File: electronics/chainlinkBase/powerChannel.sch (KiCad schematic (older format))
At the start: 15 parts, among them J201 CHANNEL, U201 INA219BxD, U202 VN7007ALH

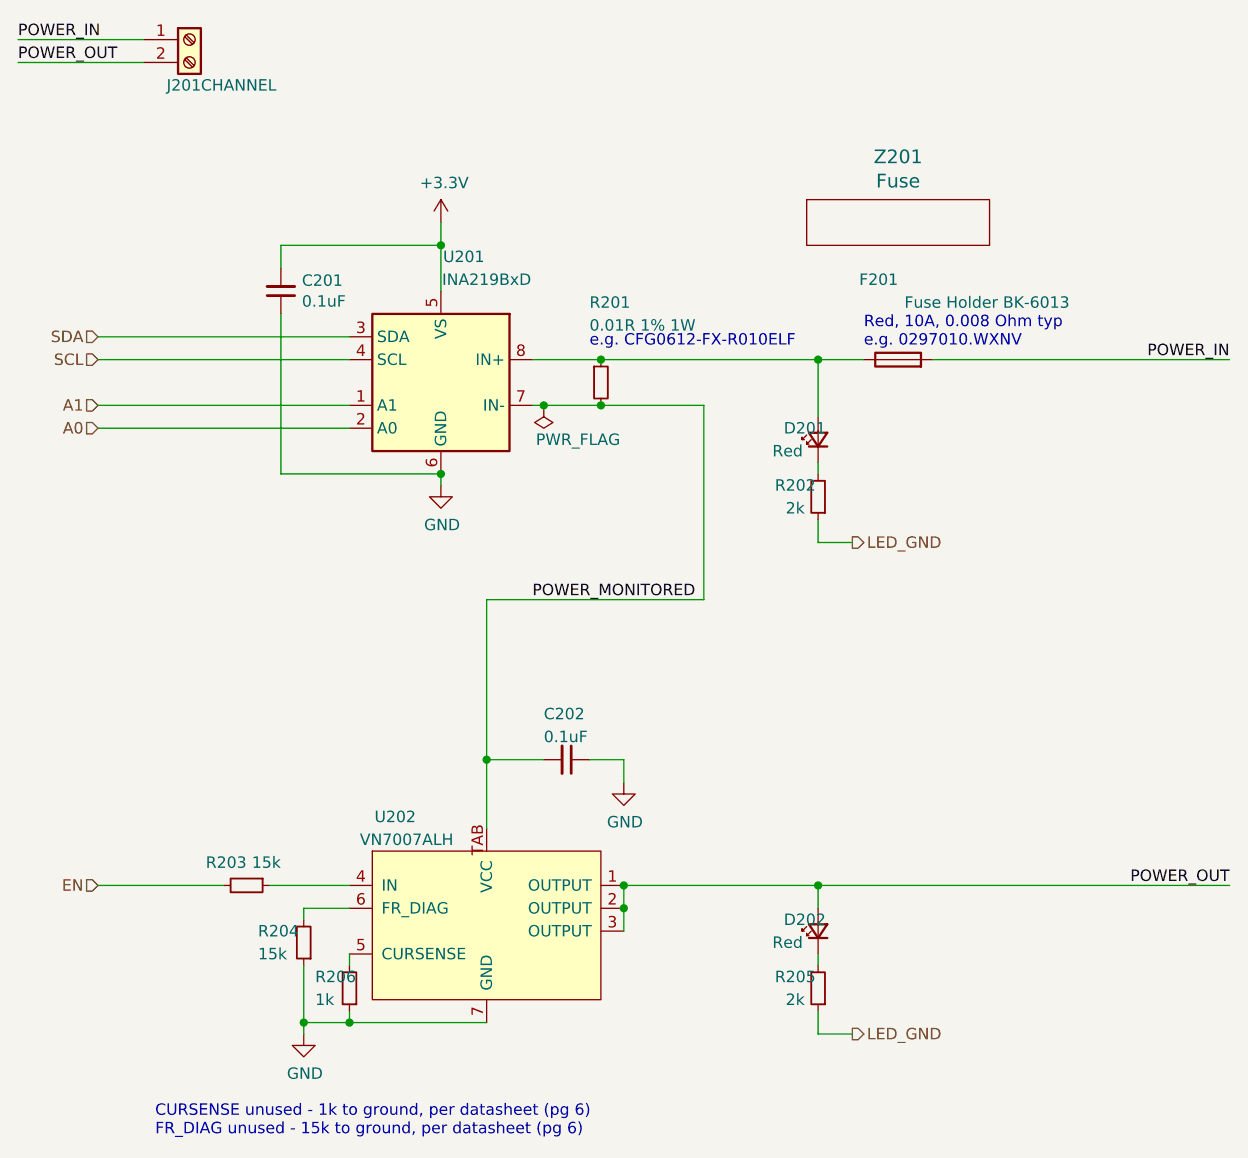
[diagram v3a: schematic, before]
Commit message: Add pull-down for load switches, move LED jumpers and make solder-bridgeable
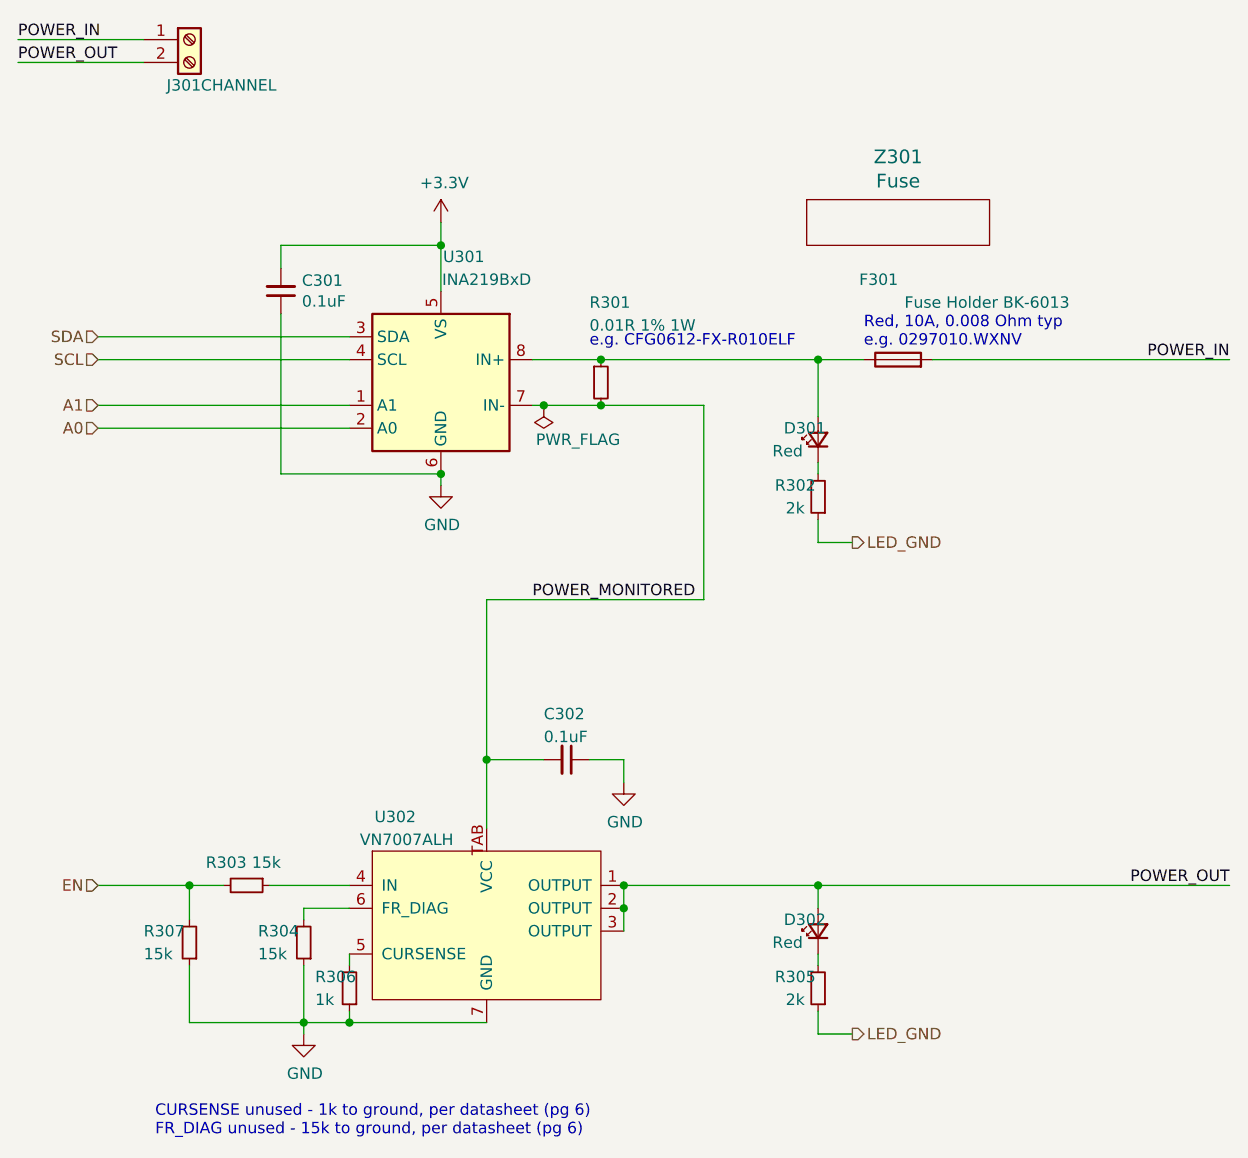
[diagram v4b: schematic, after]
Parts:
- added R207: 15k, Resistor_SMD:R_0805_2012Metric, symbol Device:R_Small
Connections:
- net EN: now also R207.2
- net GND: now also R207.1
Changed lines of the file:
@@
 $Descr A4 11693 8268
 encoding utf-8
-Sheet 2 6
+Sheet 3 6
 Title ""
 Date ""
@@
 AR Path="/60B0E338/60718742" Ref="C501"  Part="1"
 AR Path="/60B1F5E9/60718742" Ref="C601"  Part="1"
-F 0 "C201" H 2208 1804 50  0000 R CNN
+F 0 "C301" H 2208 1804 50  0000 R CNN
 F 1 "0.1uF" H 2208 1895 50  0000 R CNN
 F 2 "Capacitor_SMD:C_0805_2012Metric" H 2300 1850 50  0001 C CNN
@@
 AR Path="/60B0E338/6071874C" Ref="D502"  Part="1"
 AR Path="/60B1F5E9/6071874C" Ref="D602"  Part="1"
-F 0 "D202" V 4700 4800 50  0000 R CNN
+F 0 "D302" V 4700 4800 50  0000 R CNN
 F 1 "Red" V 4600 4850 50  0000 R CNN
 F 2 "ModifiedSymbols:LED_0805_2012Metric_Silkscreen" V 4650 4650 50  0001 C CNN
@@
 AR Path="/60B0E338/60718758" Ref="R505"  Part="1"
 AR Path="/60B1F5E9/60718758" Ref="R605"  Part="1"
-F 0 "R205" H 4750 4850 50  0000 C CNN
+F 0 "R305" H 4750 4850 50  0000 C CNN
 F 1 "2k" H 4750 4950 50  0000 C CNN
 F 2 "Resistor_SMD:R_0805_2012Metric" H 4650 4900 50  0001 C CNN
@@
 AR Path="/60B0E338/6071875F" Ref="C502"  Part="1"
 AR Path="/60B1F5E9/6071875F" Ref="C602"  Part="1"
-F 0 "C202" V 3350 3800 50  0000 L CNN
+F 0 "C302" V 3350 3800 50  0000 L CNN
 F 1 "0.1uF" V 3450 3800 50  0000 L CNN
 F 2 "Capacitor_SMD:C_0805_2012Metric" H 3550 3900 50  0001 C CNN
@@
 AR Path="/60B0E338/6071877C" Ref="R501"  Part="1"
 AR Path="/60B1F5E9/6071877C" Ref="R601"  Part="1"
-F 0 "R201" H 3650 2600 50  0000 L CNN
+F 0 "R301" H 3650 2600 50  0000 L CNN
 F 1 "0.01R 1% 1W" H 3650 2500 50  0000 L CNN
 F 2 "Resistor_SMD:R_0612_1632Metric" H 3700 2250 50  0001 C CNN
@@
 AR Path="/60B0E338/60718784" Ref="F501"  Part="1"
 AR Path="/60B1F5E9/60718784" Ref="F601"  Part="1"
-F 0 "F201" V 5350 2150 50  0000 L CNN
+F 0 "F301" V 5350 2150 50  0000 L CNN
 F 1 "Fuse Holder BK-6013" V 5250 1400 50  0000 L CNN
 F 2 "BK-6013:BK-6013" V 4930 2150 50  0001 C CNN
@@
 AR Path="/60B0E338/6071879D" Ref="R503"  Part="1"
 AR Path="/60B1F5E9/6071879D" Ref="R603"  Part="1"
-F 0 "R203" V 2050 4450 50  0000 R CNN
+F 0 "R303" V 2050 4450 50  0000 R CNN
 F 1 "15k" V 2050 4600 50  0000 R CNN
 F 2 "Resistor_SMD:R_0805_2012Metric" H 2150 4450 50  0001 C CNN
@@
 AR Path="/60B0E338/607187A4" Ref="J501"  Part="1"
 AR Path="/60B1F5E9/607187A4" Ref="J601"  Part="1"
-F 0 "J201" H 1800 550 50  0000 L CNN
+F 0 "J301" H 1800 550 50  0000 L CNN
 F 1 "CHANNEL" H 1950 550 50  0000 L CNN
 F 2 "ScrewTerminals:Generic-5.08-2P" H 1900 750 50  0001 C CNN
@@
 AR Path="/60B0E338/607187B2" Ref="U502"  Part="1"
 AR Path="/60B1F5E9/607187B2" Ref="U602"  Part="1"
-F 0 "U202" H 2800 4950 50  0000 C CNN
+F 0 "U302" H 2800 4950 50  0000 C CNN
 F 1 "VN7007ALH" H 2850 4850 50  0000 C CNN
 F 2 "VN7007ALHTR:VN7007ALHTR" H 3200 4550 50  0001 C CNN
@@
 AR Path="/60B0E338/607187BF" Ref="R506"  Part="1"
 AR Path="/60B1F5E9/607187BF" Ref="R606"  Part="1"
-F 0 "R206" H 2750 4850 50  0000 R CNN
+F 0 "R306" H 2750 4850 50  0000 R CNN
 F 1 "1k" H 2750 4950 50  0000 R CNN
 F 2 "Resistor_SMD:R_0805_2012Metric" H 2600 4900 50  0001 C CNN
@@
 AR Path="/60B0E338/607187C9" Ref="R504"  Part="1"
 AR Path="/60B1F5E9/607187C9" Ref="R604"  Part="1"
-F 0 "R204" H 2600 4650 50  0000 R CNN
+F 0 "R304" H 2600 4650 50  0000 R CNN
 F 1 "15k" H 2600 4750 50  0000 R CNN
 F 2 "Resistor_SMD:R_0805_2012Metric" H 2400 4700 50  0001 C CNN
@@
 AR Path="/60B0E338/607187E7" Ref="D501"  Part="1"
 AR Path="/60B1F5E9/607187E7" Ref="D601"  Part="1"
-F 0 "D201" V 4700 2650 50  0000 R CNN
+F 0 "D301" V 4700 2650 50  0000 R CNN
 F 1 "Red" V 4600 2700 50  0000 R CNN
 F 2 "ModifiedSymbols:LED_0805_2012Metric_Silkscreen" V 4650 2500 50  0001 C CNN
@@
 AR Path="/60B0E338/607187ED" Ref="R502"  Part="1"
 AR Path="/60B1F5E9/607187ED" Ref="R602"  Part="1"
-F 0 "R202" H 4750 2700 50  0000 C CNN
+F 0 "R302" H 4750 2700 50  0000 C CNN
 F 1 "2k" H 4750 2800 50  0000 C CNN
 F 2 "Resistor_SMD:R_0805_2012Metric" H 4650 2750 50  0001 C CNN
@@
 AR Path="/60B0E338/6071873C" Ref="U501"  Part="1"
 AR Path="/60B1F5E9/6071873C" Ref="U601"  Part="1"
-F 0 "U201" H 2900 2800 50  0000 C CNN
+F 0 "U301" H 2900 2800 50  0000 C CNN
 F 1 "INA219BxD" H 2800 2700 50  0000 C CNN
 F 2 "Package_SO:SOIC-8_3.9x4.9mm_P1.27mm" H 3800 1900 50  0001 C CNN
@@
 	3200 3200 3200 3900
 Wire Wire Line
-	1500 4450 2050 4450
+	1500 4450 1900 4450
 Wire Wire Line
 	4650 4550 4650 4450
@@
 AR Path="/60B0E338/6078F8EB" Ref="Z501"  Part="1"
 AR Path="/60B1F5E9/6078F8EB" Ref="Z601"  Part="1"
-F 0 "Z201" H 5000 1837 60  0000 C CNN
+F 0 "Z301" H 5000 1837 60  0000 C CNN
 F 1 "Fuse" H 5000 1731 60  0000 C CNN
 F 2 "Dummy:Dummy" H 5000 1550 60  0001 C CNN
@@
 	1    0    0    -1
 $EndComp
+$Comp
+L Device:R_Small R?
+U 1 1 607F8CFF
+P 1900 4700
+AR Path="/607F8CFF" Ref="R?"  Part="1"
+AR Path="/606FA86C/607F8CFF" Ref="R207"  Part="1"
+AR Path="/6077A779/607F8CFF" Ref="R?"  Part="1"
+AR Path="/60AEE6BF/607F8CFF" Ref="R307"  Part="1"
+AR Path="/60AFE278/607F8CFF" Ref="R407"  Part="1"
+AR Path="/60B0E338/607F8CFF" Ref="R507"  Part="1"
+AR Path="/60B1F5E9/607F8CFF" Ref="R607"  Part="1"
+F 0 "R307" H 2100 4650 50  0000 R CNN
+F 1 "15k" H 2100 4750 50  0000 R CNN
+F 2 "Resistor_SMD:R_0805_2012Metric" H 1900 4700 50  0001 C CNN
+F 3 "~" H 1900 4700 50  0001 C CNN
+F 4 "RMCF0805JT15K0CT-ND" H 1900 4700 50  0001 C CNN "DK#"
+	1    1900 4700
+	-1   0    0    1
+$EndComp
+Wire Wire Line
+	1900 4450 1900 4600
+Connection ~ 1900 4450
+Wire Wire Line
+	1900 4450 2050 4450
+Wire Wire Line
+	1900 4800 1900 5050
+Wire Wire Line
+	1900 5050 2400 5050
 $EndSCHEMATC

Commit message: Change Chainlink data connections from screw terminals to IDC (#189)
- Replace screw terminals with 2x4 IDC connectors (alternating ground) on Driver, Base, and Tester. Fixes #179
- Change Chainlink Driver Tester to all 1mm pogo pins
- Create new "Buddy" boards for connecting IDC/ribbon cable to T-Display or a breadboard
- Big readme cleanup and reorganization for clarity (hopefully!)
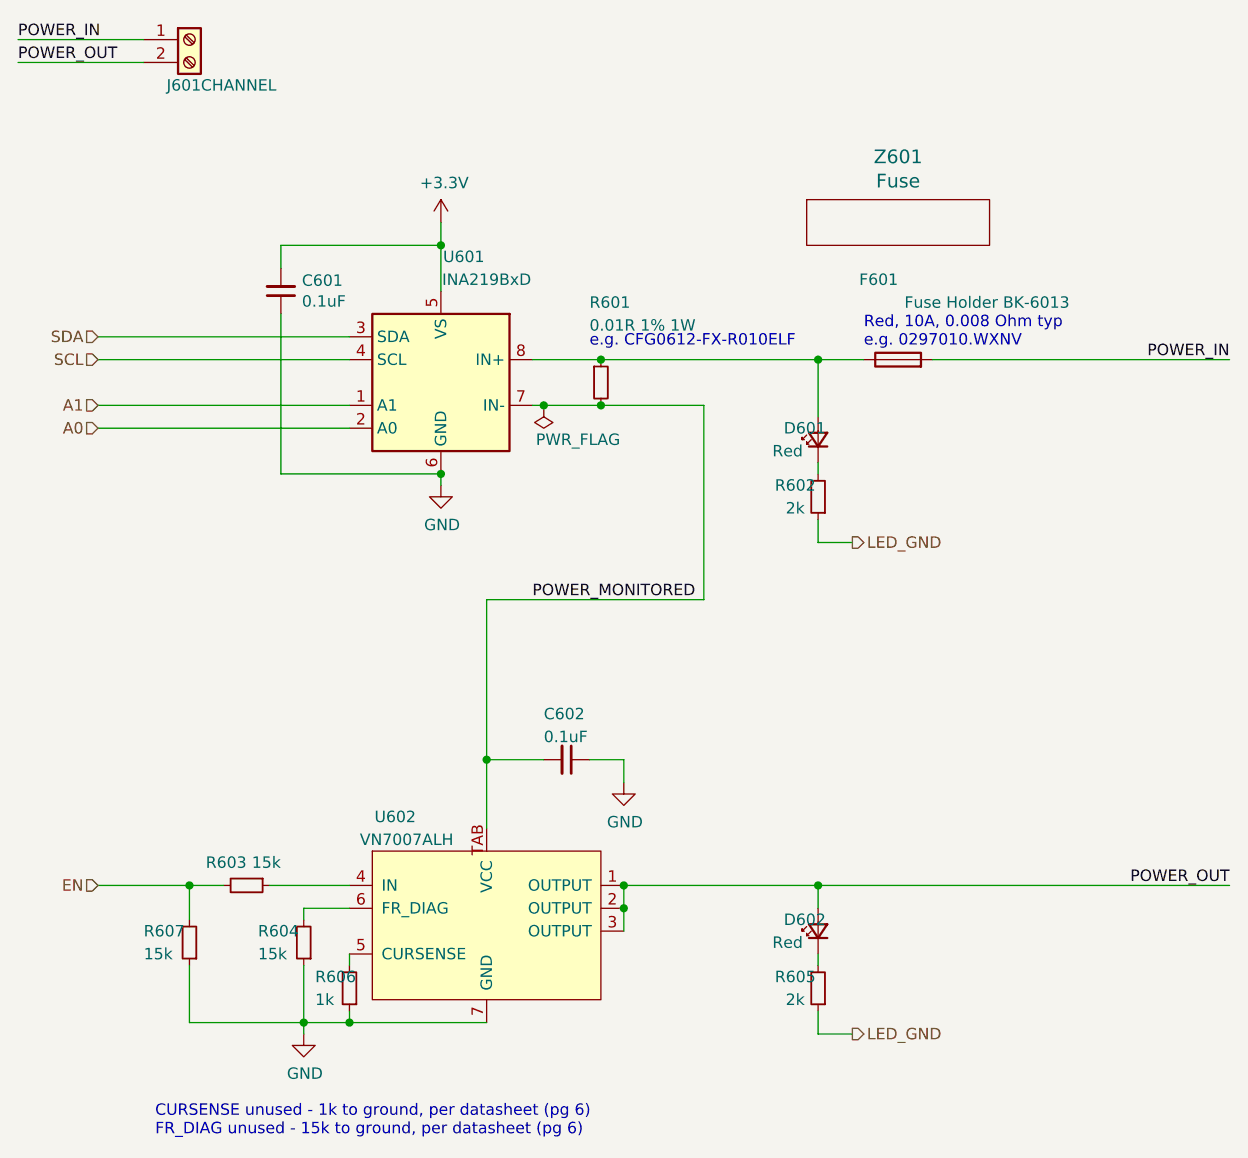
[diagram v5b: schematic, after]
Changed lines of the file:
@@
 AR Path="/60B0E338/60718742" Ref="C501"  Part="1"
 AR Path="/60B1F5E9/60718742" Ref="C601"  Part="1"
-F 0 "C301" H 2208 1804 50  0000 R CNN
+F 0 "C601" H 2208 1804 50  0000 R CNN
 F 1 "0.1uF" H 2208 1895 50  0000 R CNN
 F 2 "Capacitor_SMD:C_0805_2012Metric" H 2300 1850 50  0001 C CNN
@@
 AR Path="/60B0E338/6071874C" Ref="D502"  Part="1"
 AR Path="/60B1F5E9/6071874C" Ref="D602"  Part="1"
-F 0 "D302" V 4700 4800 50  0000 R CNN
+F 0 "D602" V 4700 4800 50  0000 R CNN
 F 1 "Red" V 4600 4850 50  0000 R CNN
 F 2 "ModifiedSymbols:LED_0805_2012Metric_Silkscreen" V 4650 4650 50  0001 C CNN
@@
 AR Path="/60B0E338/60718758" Ref="R505"  Part="1"
 AR Path="/60B1F5E9/60718758" Ref="R605"  Part="1"
-F 0 "R305" H 4750 4850 50  0000 C CNN
+F 0 "R605" H 4750 4850 50  0000 C CNN
 F 1 "2k" H 4750 4950 50  0000 C CNN
 F 2 "Resistor_SMD:R_0805_2012Metric" H 4650 4900 50  0001 C CNN
@@
 AR Path="/60B0E338/6071875F" Ref="C502"  Part="1"
 AR Path="/60B1F5E9/6071875F" Ref="C602"  Part="1"
-F 0 "C302" V 3350 3800 50  0000 L CNN
+F 0 "C602" V 3350 3800 50  0000 L CNN
 F 1 "0.1uF" V 3450 3800 50  0000 L CNN
 F 2 "Capacitor_SMD:C_0805_2012Metric" H 3550 3900 50  0001 C CNN
@@
 AR Path="/60B0E338/6071877C" Ref="R501"  Part="1"
 AR Path="/60B1F5E9/6071877C" Ref="R601"  Part="1"
-F 0 "R301" H 3650 2600 50  0000 L CNN
+F 0 "R601" H 3650 2600 50  0000 L CNN
 F 1 "0.01R 1% 1W" H 3650 2500 50  0000 L CNN
 F 2 "Resistor_SMD:R_0612_1632Metric" H 3700 2250 50  0001 C CNN
@@
 AR Path="/60B0E338/60718784" Ref="F501"  Part="1"
 AR Path="/60B1F5E9/60718784" Ref="F601"  Part="1"
-F 0 "F301" V 5350 2150 50  0000 L CNN
+F 0 "F601" V 5350 2150 50  0000 L CNN
 F 1 "Fuse Holder BK-6013" V 5250 1400 50  0000 L CNN
 F 2 "BK-6013:BK-6013" V 4930 2150 50  0001 C CNN
@@
 AR Path="/60B0E338/6071879D" Ref="R503"  Part="1"
 AR Path="/60B1F5E9/6071879D" Ref="R603"  Part="1"
-F 0 "R303" V 2050 4450 50  0000 R CNN
+F 0 "R603" V 2050 4450 50  0000 R CNN
 F 1 "15k" V 2050 4600 50  0000 R CNN
 F 2 "Resistor_SMD:R_0805_2012Metric" H 2150 4450 50  0001 C CNN
@@
 AR Path="/60B0E338/607187A4" Ref="J501"  Part="1"
 AR Path="/60B1F5E9/607187A4" Ref="J601"  Part="1"
-F 0 "J301" H 1800 550 50  0000 L CNN
+F 0 "J601" H 1800 550 50  0000 L CNN
 F 1 "CHANNEL" H 1950 550 50  0000 L CNN
 F 2 "ScrewTerminals:Generic-5.08-2P" H 1900 750 50  0001 C CNN
@@
 AR Path="/60B0E338/607187B2" Ref="U502"  Part="1"
 AR Path="/60B1F5E9/607187B2" Ref="U602"  Part="1"
-F 0 "U302" H 2800 4950 50  0000 C CNN
+F 0 "U602" H 2800 4950 50  0000 C CNN
 F 1 "VN7007ALH" H 2850 4850 50  0000 C CNN
 F 2 "VN7007ALHTR:VN7007ALHTR" H 3200 4550 50  0001 C CNN
@@
 AR Path="/60B0E338/607187BF" Ref="R506"  Part="1"
 AR Path="/60B1F5E9/607187BF" Ref="R606"  Part="1"
-F 0 "R306" H 2750 4850 50  0000 R CNN
+F 0 "R606" H 2750 4850 50  0000 R CNN
 F 1 "1k" H 2750 4950 50  0000 R CNN
 F 2 "Resistor_SMD:R_0805_2012Metric" H 2600 4900 50  0001 C CNN
@@
 AR Path="/60B0E338/607187C9" Ref="R504"  Part="1"
 AR Path="/60B1F5E9/607187C9" Ref="R604"  Part="1"
-F 0 "R304" H 2600 4650 50  0000 R CNN
+F 0 "R604" H 2600 4650 50  0000 R CNN
 F 1 "15k" H 2600 4750 50  0000 R CNN
 F 2 "Resistor_SMD:R_0805_2012Metric" H 2400 4700 50  0001 C CNN
@@
 AR Path="/60B0E338/607187E7" Ref="D501"  Part="1"
 AR Path="/60B1F5E9/607187E7" Ref="D601"  Part="1"
-F 0 "D301" V 4700 2650 50  0000 R CNN
+F 0 "D601" V 4700 2650 50  0000 R CNN
 F 1 "Red" V 4600 2700 50  0000 R CNN
 F 2 "ModifiedSymbols:LED_0805_2012Metric_Silkscreen" V 4650 2500 50  0001 C CNN
@@
 AR Path="/60B0E338/607187ED" Ref="R502"  Part="1"
 AR Path="/60B1F5E9/607187ED" Ref="R602"  Part="1"
-F 0 "R302" H 4750 2700 50  0000 C CNN
+F 0 "R602" H 4750 2700 50  0000 C CNN
 F 1 "2k" H 4750 2800 50  0000 C CNN
 F 2 "Resistor_SMD:R_0805_2012Metric" H 4650 2750 50  0001 C CNN
@@
 AR Path="/60B0E338/6071873C" Ref="U501"  Part="1"
 AR Path="/60B1F5E9/6071873C" Ref="U601"  Part="1"
-F 0 "U301" H 2900 2800 50  0000 C CNN
+F 0 "U601" H 2900 2800 50  0000 C CNN
 F 1 "INA219BxD" H 2800 2700 50  0000 C CNN
 F 2 "Package_SO:SOIC-8_3.9x4.9mm_P1.27mm" H 3800 1900 50  0001 C CNN
@@
 AR Path="/60B0E338/6078F8EB" Ref="Z501"  Part="1"
 AR Path="/60B1F5E9/6078F8EB" Ref="Z601"  Part="1"
-F 0 "Z301" H 5000 1837 60  0000 C CNN
+F 0 "Z601" H 5000 1837 60  0000 C CNN
 F 1 "Fuse" H 5000 1731 60  0000 C CNN
 F 2 "Dummy:Dummy" H 5000 1550 60  0001 C CNN
@@
 AR Path="/60B0E338/607F8CFF" Ref="R507"  Part="1"
 AR Path="/60B1F5E9/607F8CFF" Ref="R607"  Part="1"
-F 0 "R307" H 2100 4650 50  0000 R CNN
+F 0 "R607" H 2100 4650 50  0000 R CNN
 F 1 "15k" H 2100 4750 50  0000 R CNN
 F 2 "Resistor_SMD:R_0805_2012Metric" H 1900 4700 50  0001 C CNN
